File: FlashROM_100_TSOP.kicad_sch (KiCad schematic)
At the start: 6 parts

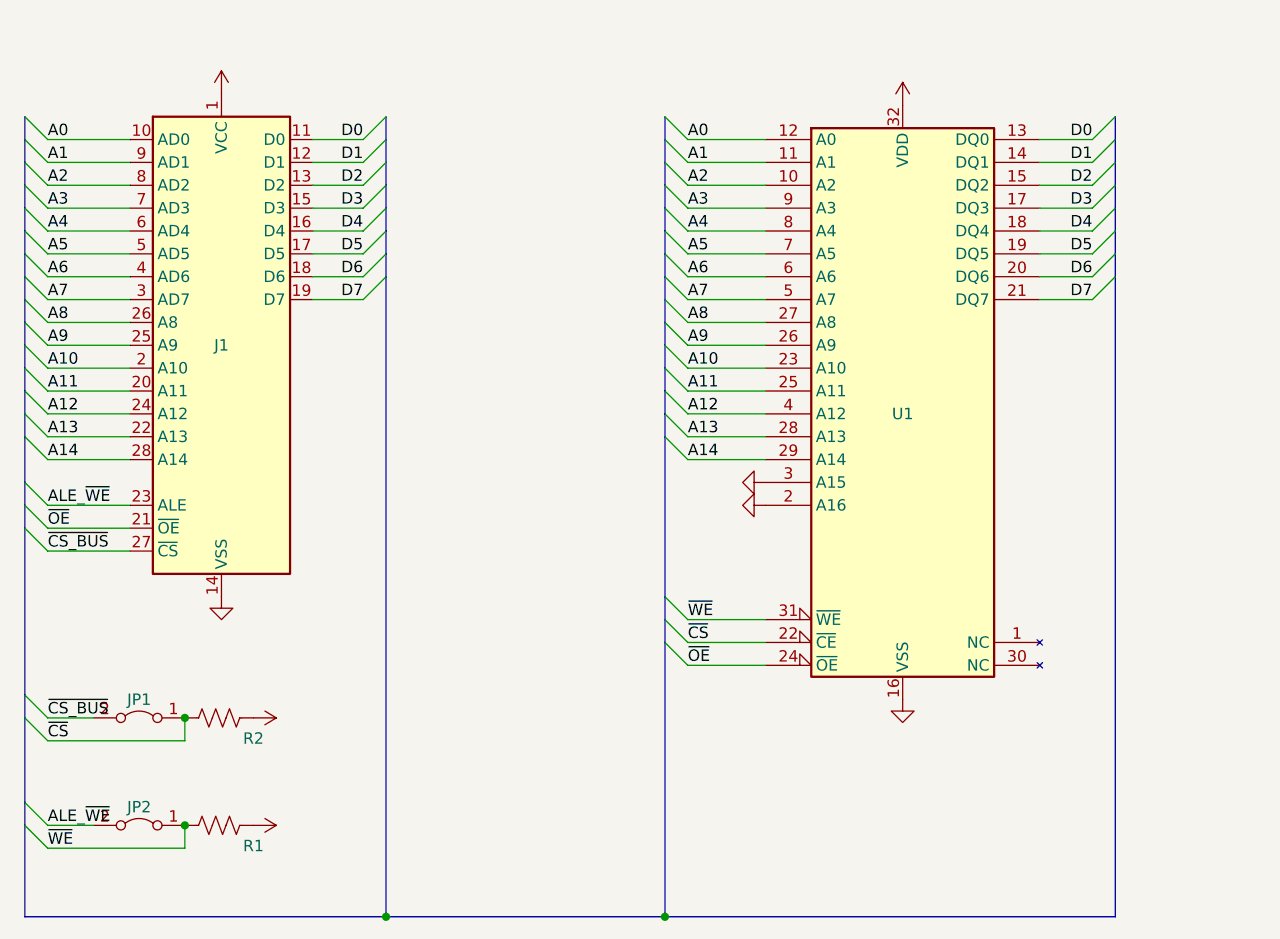
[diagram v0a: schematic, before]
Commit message: Fix wrong pinout on FlashROM_100 TSOPgit add -A!
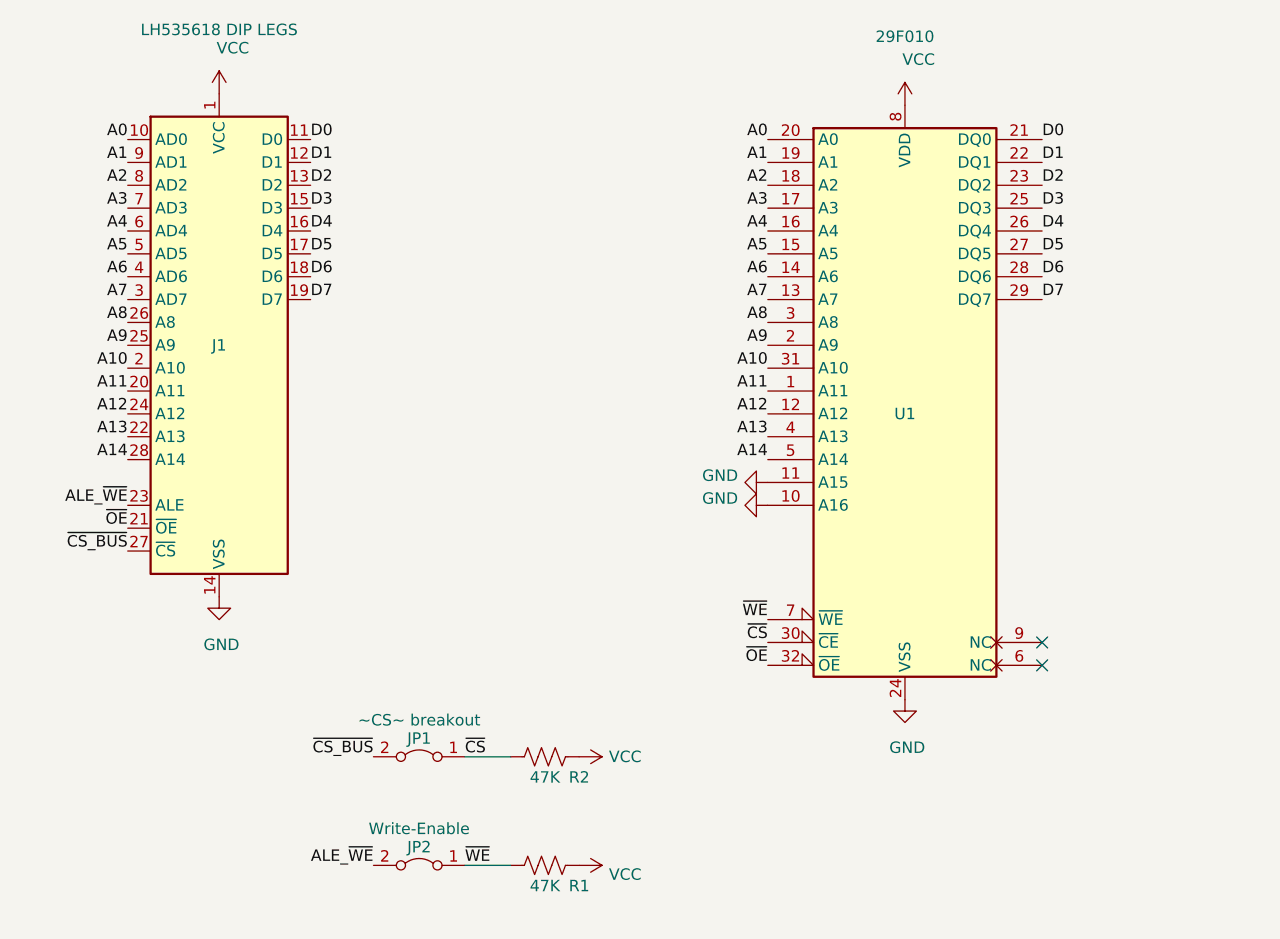
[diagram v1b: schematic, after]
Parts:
- J1: value (none) -> LH535618 DIP LEGS; footprint (none) -> 000_LOCAL:DIP28_0.6_pcb
- JP1: value (none) -> ~CS~ breakout; footprint (none) -> 000_LOCAL:Pin_Header_Angled_1x02_Pitch2.54mm
- JP2: value (none) -> Write-Enable; footprint (none) -> 000_LOCAL:Pin_Header_Angled_1x02_Pitch2.54mm
- R1, R2: value (none) -> 47K; footprint (none) -> 000_LOCAL:R_0805
- U1: value (none) -> 29F010; footprint (none) -> 000_LOCAL:TSOP32-14mm; symbol 000_LOCAL:SST39SF010_PLCC -> 000_LOCAL:SST39SF010_TSOP
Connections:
- net A0: now also U1.20 (A0); no longer U1.12 (A0)
- net A1: now also U1.19 (A1); no longer U1.11 (A1)
- net A10: now also U1.31 (A10); no longer U1.23 (A10)
- net A11: now also U1.1 (A11); no longer U1.25 (A11)
- net A12: now also U1.12 (A12); no longer U1.4 (A12)
- net A13: now also U1.4 (A13); no longer U1.28 (A13)
- net A14: now also U1.5 (A14); no longer U1.29 (A14)
- net A2: now also U1.18 (A2); no longer U1.10 (A2)
- net A3: now also U1.17 (A3); no longer U1.9 (A3)
- net A4: now also U1.16 (A4); no longer U1.8 (A4)
- net A5: now also U1.15 (A5); no longer U1.7 (A5)
- net A6: now also U1.14 (A6); no longer U1.6 (A6)
- net A7: now also U1.13 (A7); no longer U1.5 (A7)
- net A8: now also U1.3 (A8); no longer U1.27 (A8)
- net A9: now also U1.2 (A9); no longer U1.26 (A9)
- net D0: now also U1.21 (DQ0); no longer U1.13 (DQ0)
- net D1: now also U1.22 (DQ1); no longer U1.14 (DQ1)
- net D2: now also U1.23 (DQ2); no longer U1.15 (DQ2)
- net D3: now also U1.25 (DQ3); no longer U1.17 (DQ3)
- net D4: now also U1.26 (DQ4); no longer U1.18 (DQ4)
- net D5: now also U1.27 (DQ5); no longer U1.19 (DQ5)
- net D6: now also U1.28 (DQ6); no longer U1.20 (DQ6)
- net D7: now also U1.29 (DQ7); no longer U1.21 (DQ7)
- net GND: now also U1.10 (A16), U1.11 (A15), U1.24 (VSS); no longer U1.16 (VSS), U1.2 (A16), U1.3 (A15)
- net VCC: now also U1.8 (VDD); no longer U1.32 (VDD)
- net ~{CS}: now also U1.30 (~{CE}); no longer U1.22 (~{CE})
- net ~{OE}: now also U1.32 (~{OE}); no longer U1.24 (~{OE})
- net ~{WE}: now also U1.7 (~{WE}); no longer U1.31 (~{WE})
- no-connect marks 0 -> 2
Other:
- moved on the sheet: JP1, JP2, R1, R2

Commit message: dual tsop footprint on flashrom_100
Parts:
- U1: footprint 000_LOCAL:TSOP32-14mm -> 000_LOCAL:TSOP32-dual
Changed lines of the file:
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@@
     (property "Reference" "U1" (id 0) (at 173.99 88.9 0))
     (property "Value" "29F010" (id 1) (at 173.99 46.99 0))
-    (property "Footprint" "000_LOCAL:TSOP32-14mm" (id 2) (at 173.99 81.28 0)
+    (property "Footprint" "000_LOCAL:TSOP32-dual" (id 2) (at 173.99 81.28 0)
       (effects (font (size 1.27 1.27)) hide)
     )
@@
     )
     (path "/00000000-0000-0000-0000-00005e5b130a"
-      (reference "U1") (unit 1) (value "29F010") (footprint "000_LOCAL:TSOP32-14mm")
-    )
-  )
+      (reference "U1") (unit 1) (value "29F010") (footprint "000_LOCAL:TSOP32-dual")
+    )
+  )

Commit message: various minor cleanups
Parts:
- JP1: value ~CS~ breakout -> ~{CS} breakout
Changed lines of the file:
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@@
   (title_block
     (title "FlashROM_100 - TSOP")
-    (date "2022-10-11")
-    (rev "003")
+    (date "2022-10-12")
+    (rev "004")
     (company "Brian K. White - b.kenyon.w@gmail.com")
     (comment 1 "TRS-80 Model 100 system rom with suport for REX main rom feature")
@@
     (in_bom yes) (on_board yes)
     (property "Reference" "JP1" (id 0) (at 120.015 124.968 0))
-    (property "Value" "~CS~ breakout" (id 1) (at 120.015 122.936 0))
+    (property "Value" "~{CS} breakout" (id 1) (at 120.015 122.936 0))
     (property "Footprint" "000_LOCAL:Pin_Header_Angled_1x02_Pitch2.54mm" (id 2) (at 120.015 127 0)
       (effects (font (size 1.27 1.27)) hide)
@@
     )
     (path "/00000000-0000-0000-0000-00005e68b8a2"
-      (reference "JP1") (unit 1) (value "~CS~ breakout") (footprint "000_LOCAL:Pin_Header_Angled_1x02_Pitch2.54mm")
+      (reference "JP1") (unit 1) (value "~{CS} breakout") (footprint "000_LOCAL:Pin_Header_Angled_1x02_Pitch2.54mm")
     )
     (path "/00000000-0000-0000-0000-00005fbc3795"

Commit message: minor touches
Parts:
- R1, R2: value 47K -> 100K
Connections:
- net ~{CS} renamed ~{CS_IC}
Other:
- note added: "AM29F010 SST39SF010A AS29CF010 AT29C010A GLS27SF010 28F001 28C010"
- title: FlashROM_100 - TSOP -> FlashROM_100_TSOP
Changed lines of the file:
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@@
   (paper "USLetter")
   (title_block
-    (title "FlashROM_100 - TSOP")
-    (date "2022-10-12")
-    (rev "004")
+    (title "FlashROM_100_TSOP")
+    (date "2023-02-23")
+    (rev "006")
     (company "Brian K. White - b.kenyon.w@gmail.com")
     (comment 1 "TRS-80 Model 100 system rom with suport for REX main rom feature")
@@
     (stroke (width 0) (type default) (color 0 0 0 0))
   )
+  (text "AM29F010\nSST39SF010A\nAS29CF010\nAT29C010A\nGLS27SF010\n28F001\n28C010"
+    (at 199.39 106.68 0)
+    (effects (font (size 1.27 1.27)) (justify left bottom))
+  )
   (label "D1" (at 189.23 60.96 0)
     (effects (font (size 1.27 1.27)) (justify left bottom))
@@
     (effects (font (size 1.27 1.27)) (justify right bottom))
   )
-  (label "~{CS}" (at 125.095 127 0)
+  (label "~{CS_IC}" (at 125.095 127 0)
     (effects (font (size 1.27 1.27)) (justify left bottom))
   )
@@
     (effects (font (size 1.27 1.27)) (justify left bottom))
   )
-  (label "~{CS}" (at 158.75 114.3 180)
+  (label "~{CS_IC}" (at 158.75 114.3 180)
     (effects (font (size 1.27 1.27)) (justify right bottom))
   )
@@
       (effects (font (size 1.27 1.27)) hide)
     )
-    (property "Datasheet" "http://ww1.microchip.com/downloads/en/DeviceDoc/25022B.pdf" (id 3) (at 173.99 88.9 0)
+    (property "Datasheet" "https://ww1.microchip.com/downloads/aemDocuments/documents/OTH/ProductDocuments/DataSheets/20005022C.pdf" (id 3) (at 173.99 88.9 0)
       (effects (font (size 1.27 1.27)) hide)
     )
@@
     (in_bom yes) (on_board yes)
     (property "Reference" "R2" (id 0) (at 137.795 129.286 90))
-    (property "Value" "47K" (id 1) (at 133.985 129.286 90))
+    (property "Value" "100K" (id 1) (at 133.985 129.286 90))
     (property "Footprint" "000_LOCAL:R_0805" (id 2) (at 133.985 127 0)
       (effects (font (size 1.27 1.27)) hide)
@@
     (in_bom yes) (on_board yes)
     (property "Reference" "R1" (id 0) (at 137.795 141.351 90))
-    (property "Value" "47K" (id 1) (at 133.985 141.351 90))
+    (property "Value" "100K" (id 1) (at 133.985 141.351 90))
     (property "Footprint" "000_LOCAL:R_0805" (id 2) (at 133.985 139.065 0)
       (effects (font (size 1.27 1.27)) hide)
@@
     )
     (path "/00000000-0000-0000-0000-00005e6b3af8"
-      (reference "R1") (unit 1) (value "47K") (footprint "000_LOCAL:R_0805")
+      (reference "R1") (unit 1) (value "100K") (footprint "000_LOCAL:R_0805")
     )
     (path "/00000000-0000-0000-0000-00005e68c7f8"
-      (reference "R2") (unit 1) (value "47K") (footprint "000_LOCAL:R_0805")
+      (reference "R2") (unit 1) (value "100K") (footprint "000_LOCAL:R_0805")
     )
     (path "/00000000-0000-0000-0000-00005e5b130a"
